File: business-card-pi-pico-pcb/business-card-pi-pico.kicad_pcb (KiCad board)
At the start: 2 copper layers, 2 parts, among them U1 Pico

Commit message: continued working on PCB
continued working on PCB
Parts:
- added D1: LED, LED_SMD:LED_0805_2012Metric, F.Cu at (121.5, 63.5)
- added D10: LED, LED_SMD:LED_0805_2012Metric, F.Cu at (97.8, 73.5)
- added D11: LED, LED_SMD:LED_0805_2012Metric, F.Cu at (97.8, 76.5)
- added D12: LED, LED_SMD:LED_0805_2012Metric, F.Cu at (97.8, 79.6)
- added D13: LED, LED_SMD:LED_0805_2012Metric, F.Cu at (97.8, 82.6)
- added D14: LED, LED_SMD:LED_0805_2012Metric, F.Cu at (102.3, 61.3)
- added D15: LED, LED_SMD:LED_0805_2012Metric, F.Cu at (102.3, 64.4)
- added D16: LED, LED_SMD:LED_0805_2012Metric, F.Cu at (102.3, 67.4)
- added D17: LED, LED_SMD:LED_0805_2012Metric, F.Cu at (102.3, 70.5)
- added D18: LED, LED_SMD:LED_0805_2012Metric, F.Cu at (102.3, 73.5)
- added D19: LED, LED_SMD:LED_0805_2012Metric, F.Cu at (102.3, 76.5)
- added D2: LED, LED_SMD:LED_0805_2012Metric, F.Cu at (120.1, 69.9)
- added D20: LED, LED_SMD:LED_0805_2012Metric, F.Cu at (102.3, 79.6)
- added D21: LED, LED_SMD:LED_0805_2012Metric, F.Cu at (102.3, 82.6)
- added D22: LED, LED_SMD:LED_0805_2012Metric, F.Cu at (106.7, 61.3)
- added D23: LED, LED_SMD:LED_0805_2012Metric, F.Cu at (106.7, 64.4)
- added D24: LED, LED_SMD:LED_0805_2012Metric, F.Cu at (106.7, 67.4)
- added D25: LED, LED_SMD:LED_0805_2012Metric, F.Cu at (106.7, 70.5)
- added D26: LED, LED_SMD:LED_0805_2012Metric, F.Cu at (106.7, 73.5)
- added D27: LED, LED_SMD:LED_0805_2012Metric, F.Cu at (106.7, 76.5)
- added D28: LED, LED_SMD:LED_0805_2012Metric, F.Cu at (106.7, 79.6)
- added D29: LED, LED_SMD:LED_0805_2012Metric, F.Cu at (106.7, 82.6)
- added D3: LED, LED_SMD:LED_0805_2012Metric, F.Cu at (120.1, 72.9)
- added D30: LED, LED_SMD:LED_0805_2012Metric, F.Cu at (111.2, 61.3)
- added D31: LED, LED_SMD:LED_0805_2012Metric, F.Cu at (111.2, 64.4)
- added D32: LED, LED_SMD:LED_0805_2012Metric, F.Cu at (111.2, 67.4)
- added D33: LED, LED_SMD:LED_0805_2012Metric, F.Cu at (111.2, 70.5)
- added D34: LED, LED_SMD:LED_0805_2012Metric, F.Cu at (111.2, 73.5)
- added D35: LED, LED_SMD:LED_0805_2012Metric, F.Cu at (111.2, 76.5)
- added D36: LED, LED_SMD:LED_0805_2012Metric, F.Cu at (111.2, 79.6)
- added D4: LED, LED_SMD:LED_0805_2012Metric, F.Cu at (120.1, 76.0)
- added D5: LED, LED_SMD:LED_0805_2012Metric, F.Cu at (120.1, 79.0)
- added D6: LED, LED_SMD:LED_0805_2012Metric, F.Cu at (97.8, 61.3)
- added D7: LED, LED_SMD:LED_0805_2012Metric, F.Cu at (97.8, 64.4)
- added D8: LED, LED_SMD:LED_0805_2012Metric, F.Cu at (97.8, 67.4)
- added D9: LED, LED_SMD:LED_0805_2012Metric, F.Cu at (97.8, 70.5)
- added R1: R, Resistor_SMD:R_0805_2012Metric, F.Cu at (155.1, 56.0)
- added R2: R, Resistor_SMD:R_0805_2012Metric, F.Cu at (155.1, 58.5)
- added R3: R, Resistor_SMD:R_0805_2012Metric, F.Cu at (155.1, 63.5)
- added R4: R, Resistor_SMD:R_0805_2012Metric, F.Cu at (155.1, 66.0)
- added R5: R, Resistor_SMD:R_0805_2012Metric, F.Cu at (155.1, 68.5)
- added R6: R, Resistor_SMD:R_0805_2012Metric, F.Cu at (155.1, 71.0)
- added R7: R, Resistor_SMD:R_0805_2012Metric, F.Cu at (155.0, 76.0)
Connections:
- U1 pad 1: unconnected-(U1-GPIO0-Pad1) -> pin1
- U1 pad 2: unconnected-(U1-GPIO1-Pad2) -> pin2
- U1 pad 4: unconnected-(U1-GPIO2-Pad4) -> pin3
- U1 pad 5: unconnected-(U1-GPIO3-Pad5) -> pin4
- U1 pad 6: unconnected-(U1-GPIO4-Pad6) -> pin5
- U1 pad 7: unconnected-(U1-GPIO5-Pad7) -> pin6
- U1 pad 9: unconnected-(U1-GPIO6-Pad9) -> pin7

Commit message: PCB updated a bit
PCB updated a bit
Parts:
- removed BT1: Battery_Cell, Battery:Battery_Panasonic_CR2032-HFN_Horizontal_CircularHoles
- moved R3 63.5 mm to (91.6, 61.2), turned to 0 degrees
- moved R4 63.5 mm to (91.6, 64.2), turned to 0 degrees
- moved R5 63.5 mm to (91.6, 67.1), turned to 0 degrees
- moved R6 63.5 mm to (91.6, 70.0), turned to 0 degrees
- moved R1 63.5 mm to (91.6, 55.3), turned to 0 degrees
- moved R2 63.5 mm to (91.6, 58.2), turned to 0 degrees
- moved R7 63.5 mm to (91.6, 73.0), turned to 0 degrees
- moved D10 24.7 mm to (73.8, 67.5)
- moved D11 24.7 mm to (73.8, 70.5)
- moved D12 24.7 mm to (73.8, 73.6)
- moved D13 24.7 mm to (73.8, 76.6)
- moved D14 24.7 mm to (78.3, 55.3)
- moved D15 24.7 mm to (78.3, 58.4)
- moved D16 24.7 mm to (78.3, 61.4)
- moved D17 24.7 mm to (78.3, 64.5)
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
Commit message: added SSD13006 display
added SSD13006 display and push button
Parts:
- added J1: Conn_01x04_Pin, Display:Adafruit_SSD1306, F.Cu at (113.1, 58.5)
- added SW1: SW_Push, Button_Switch_THT:SW_PUSH_6mm_H8mm, F.Cu at (145.5, 98.0)

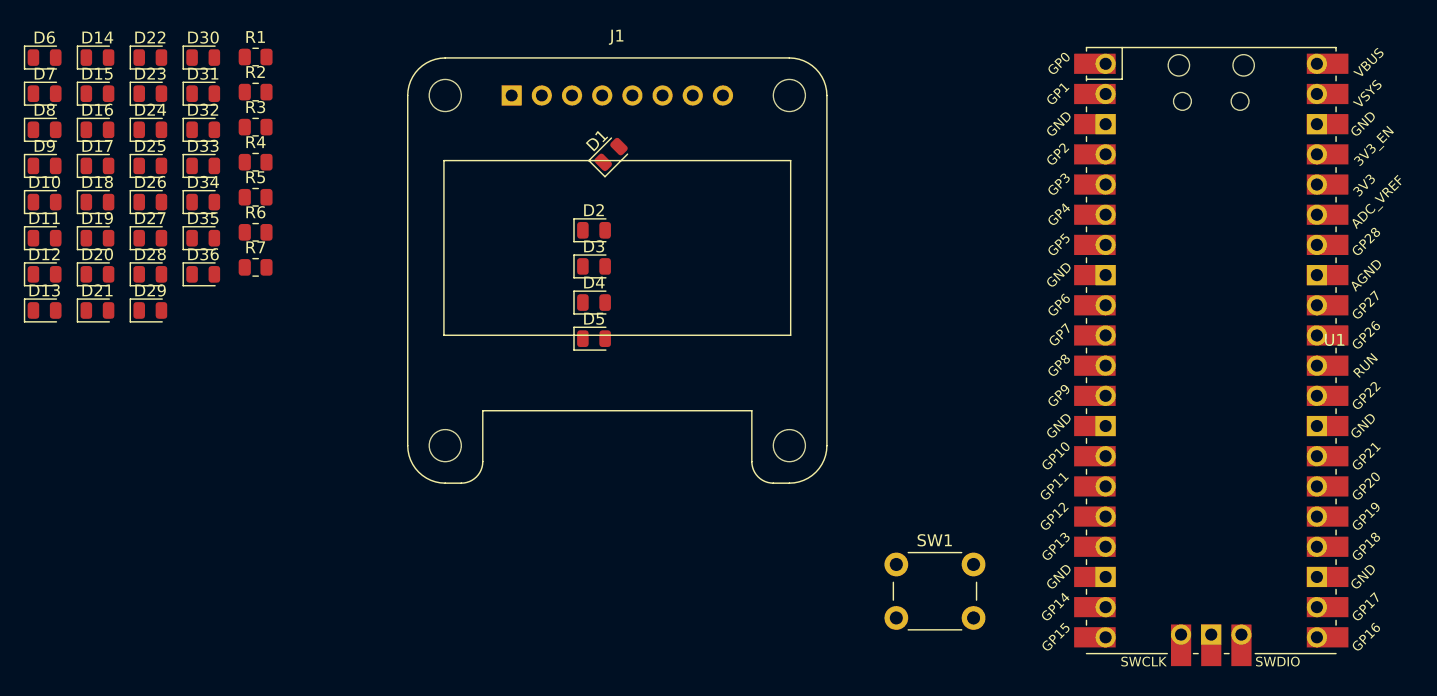
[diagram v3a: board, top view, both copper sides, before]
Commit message: Continue working on PCB
Continue working on PCB, added button/touch input pin
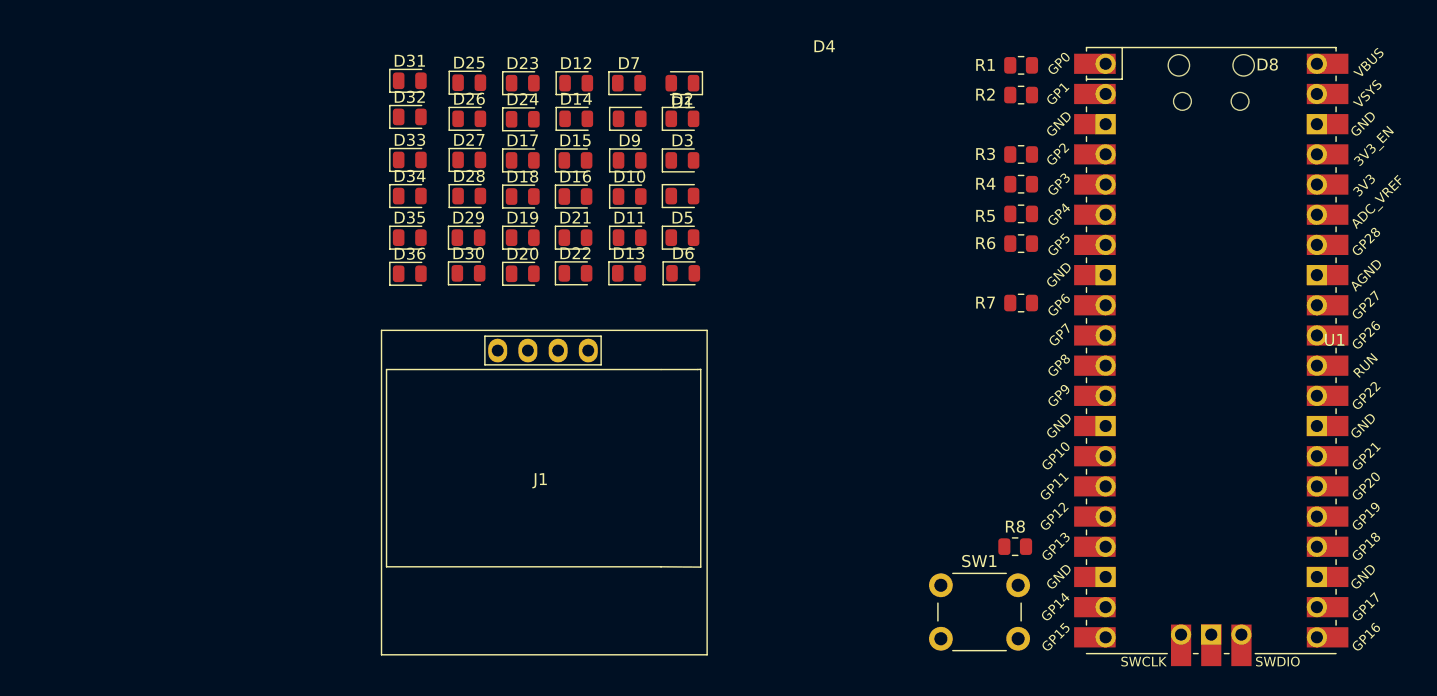
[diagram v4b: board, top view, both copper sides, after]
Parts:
- added R8: R, Resistor_SMD:R_0805_2012Metric, F.Cu at (155.5, 96.5)
- J1: footprint Display:Adafruit_SSD1306 -> SSD1306:128x64OLED
- moved R7 64.5 mm to (156.0, 76.0)
- moved R3 64.5 mm to (156.0, 63.5)
- moved R4 64.4 mm to (156.0, 66.0)
- moved R5 64.4 mm to (156.0, 68.5)
- moved R6 64.4 mm to (156.0, 71.0)
- moved R1 64.4 mm to (156.0, 56.0)
- moved R2 64.4 mm to (156.0, 58.5)
- moved D6 56.7 mm to (127.6, 73.5)
- moved D13 49.3 mm to (123.0, 73.5)
- moved D8 49.2 mm to (123.1, 60.5)
- moved D10 49.2 mm to (123.1, 67.0)
- moved D9 49.2 mm to (123.1, 64.0)
- moved D11 49.2 mm to (123.1, 70.5)
- moved D7 49.2 mm to (123.0, 57.5)
- moved D12 47.5 mm to (118.6, 57.5)
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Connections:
- J1 pad 1: unconnected-(J1-Pin_1-Pad1) -> SDA
- J1 pad 2: unconnected-(J1-Pin_2-Pad2) -> SCL
- J1 pad 3: unconnected-(J1-Pin_3-Pad3) -> 3V3
- J1 pad 4: unconnected-(J1-Pin_4-Pad4) -> GND
- SW1 pad 1: unconnected-(SW1-Pad1) -> GND
- SW1 pad 2: unconnected-(SW1-Pad2) -> Capacitive_touch
- U1 pad 10: unconnected-(U1-GPIO7-Pad10) -> Capacitive_touch
- U1 pad 13: unconnected-(U1-GND-Pad13) -> GND
- U1 pad 14: unconnected-(U1-GPIO10-Pad14) -> SDA
- U1 pad 15: unconnected-(U1-GPIO11-Pad15) -> SCL
- U1 pad 18: unconnected-(U1-GND-Pad18) -> GND
- U1 pad 23: unconnected-(U1-GND-Pad23) -> GND
- U1 pad 28: unconnected-(U1-GND-Pad28) -> GND
- U1 pad 3: unconnected-(U1-GND-Pad3) -> GND
- U1 pad 36: unconnected-(U1-3V3-Pad36) -> 3V3
- U1 pad 38: unconnected-(U1-GND-Pad38) -> GND
- U1 pad 42: unconnected-(U1-GND-Pad42) -> GND
- U1 pad 8: unconnected-(U1-GND-Pad8) -> GND

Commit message: updated PCB
updated PCB
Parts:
- added R9: R, Resistor_SMD:R_0805_2012Metric, F.Cu at (154.5, 92.4)
- moved J1 1.10 mm to (115.6, 89.5)
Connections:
- R8 pad 1: Capacitive_touch -> Net-(R8-Pad1)
- SW1 pad 2: Capacitive_touch -> Net-(R8-Pad1)
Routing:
- net 3V3: track 0.00 -> 45.3 mm
- net Net-(R8-Pad1): track 0.00 -> 35.8 mm
- net GND: vias 0 -> 6
- added copper zone on F.Cu, net GND
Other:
- board text added: "Hour (ex: 00101= 5h)"
- board text added: "Minute (ex: 100000= 32min)"
- board text added: "Temp (ex: 10000= 16C)"
- board text added: "Touch Me"

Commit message: design finished
design finished, sent PCB to fab at JLCPCB
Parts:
- moved D31 0.20 mm to (104.6, 57.5), turned to 180 degrees
- moved D32 0.16 mm to (104.6, 60.5)
- turned D13 to 180 degrees
- turned D14 to 180 degrees
- turned D16 to 180 degrees
- turned D17 to 180 degrees
- turned D20 to 180 degrees
- turned D22 to 180 degrees
- turned D23 to 180 degrees
- turned D26 to 180 degrees
- turned D28 to 180 degrees
- turned D30 to 180 degrees
- turned D34 to 180 degrees
- turned D36 to 180 degrees
- turned D4 to 180 degrees
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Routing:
- net Net-(D10-K): track 0.00 -> 98.3 mm, vias 0 -> 4
- net Net-(D1-K): track 0.00 -> 88.6 mm, vias 0 -> 2
- net Net-(D1-A): track 0.00 -> 88.0 mm, vias 0 -> 2
- net Net-(D17-K): track 0.00 -> 83.1 mm, vias 0 -> 5
- net Net-(D11-K): track 0.00 -> 81.3 mm, vias 0 -> 2
- net Net-(D12-A): track 0.00 -> 75.7 mm, vias 0 -> 5
- net Net-(D10-A): track 0.00 -> 59.8 mm, vias 0 -> 2
- net SCL: track 0.00 -> 59.0 mm, vias 0 -> 1
- net SDA: track 0.00 -> 57.4 mm, vias 0 -> 1
- net 3V3: track 45.3 -> 99.4 mm
- net Capacitive_touch: track 0.00 -> 20.3 mm, vias 0 -> 1
- net GND: track 0.00 -> 7.01 mm
- net pin7: track 0.00 -> 6.28 mm
- net pin1: track 0.00 -> 6.25 mm
- net pin6: track 0.00 -> 6.24 mm
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- added copper zone on B.Cu, net GND
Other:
- board outline added: 85 x 54 mm
- board text added: "Contact info: Fritzen, Clovis https://FritzenLab.com.br https://FritzenLab.net clovisf@gmail.com"
- board text added: "Hour (e.g: 00101= 5h)"
- board text added: "Minute (e.g: 100000= 32min)"
- board text added: "Temp (e.g: 10000= 16C)"
- board text removed: "Hour (ex: 00101= 5h)"
- board text removed: "Minute (ex: 100000= 32min)"
- board text removed: "Temp (ex: 10000= 16C)"

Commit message: backups
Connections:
- J1 pad 1: SDA -> 3V3
- J1 pad 2: SCL -> GND
- J1 pad 3: 3V3 -> SCL
- J1 pad 4: GND -> SDA
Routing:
- net SDA: track 57.4 -> 51.9 mm, vias 1 -> 0
- net SCL: track 59.0 -> 53.7 mm, vias 1 -> 0
- net 3V3: track 99.4 -> 104.5 mm
